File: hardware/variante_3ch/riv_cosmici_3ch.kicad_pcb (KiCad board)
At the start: 2 copper layers, 103 x 223.9 mm, 214 parts, among them J101 SiPM_CH1, J104 LEMO_CH1, J201 SiPM_CH2, J204 LEMO_CH2, J3 PWR_5V, J301 SiPM_CH3, J304 LEMO_CH3, J5 LEMO_AND, J6 I2C_RPI, Q101 BFR93A, Q102 MMBTH81, Q201 BFR93A, Q202 MMBTH81, Q301 BFR93A, Q302 MMBTH81, U1 LT3461, U10 74LVC1G11, U102 TLC555/LMC555, U103 MAX961, U108 LT1636, U109 74LVC1G17, U11 MCP3424, U12 MCP3424, U202 TLC555/LMC555, U203 MAX961, U208 LT1636, U209 74LVC1G17, U302 TLC555/LMC555, U303 MAX961, U308 LT1636, U309 74LVC1G17, U5 LP2985AIM5-3.6, U6 MCP1825S-3302, U7 LP2985AIM5-3.6

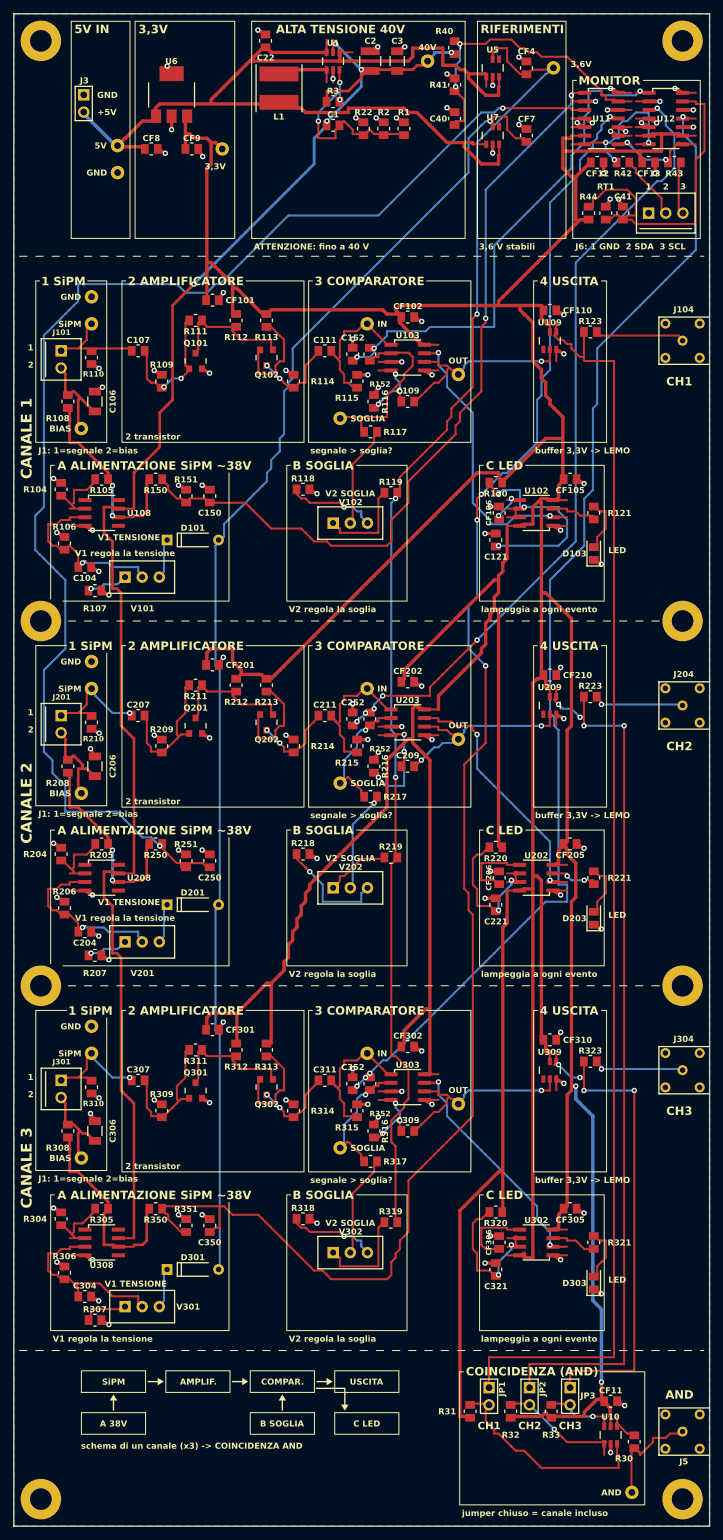
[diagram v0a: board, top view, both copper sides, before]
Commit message: Scheda a 3 canali: protezione dell'alimentazione (USB-C, fusibile, TVS, MOSFET P, LED)
USB-C solo alimentazione J7 (GCT USB4125-GF-A, 5,1k su CC) o J3 da banco ->
fusibile ripristinabile F1 (MF-MSMF050-2) -> TVS D5 (SMAJ5.0A) -> MOSFET P Q4
(AO3401A, inversione di polarita') -> +5V; C60 10 uF e LED di accensione D6.
Generatore: piazzole con asola (guscio USB-C) in PCB KiCad, Gerber e foratura (G85);
nuovi simboli e impronte (dalla libreria KiCad 7.0.11); routing aggiunto senza toccare
le altre reti. Verifica KiCad: schema = PCB, DRC senza errori, 0 reti spezzate.
Simulazione ngspice della scheda intera: +5V 4,977 V, il resto invariato.
Schema A4: nuovo foglio 2 (ingresso e protezione); nota per il tecnico INFN aggiornata.

Co-Authored-By: Claude Opus 5.5 <noreply@anthropic.com>
Claude-Session: https://claude.ai/code/session_017fc9yPsNewCQrMK8R1c8Ls
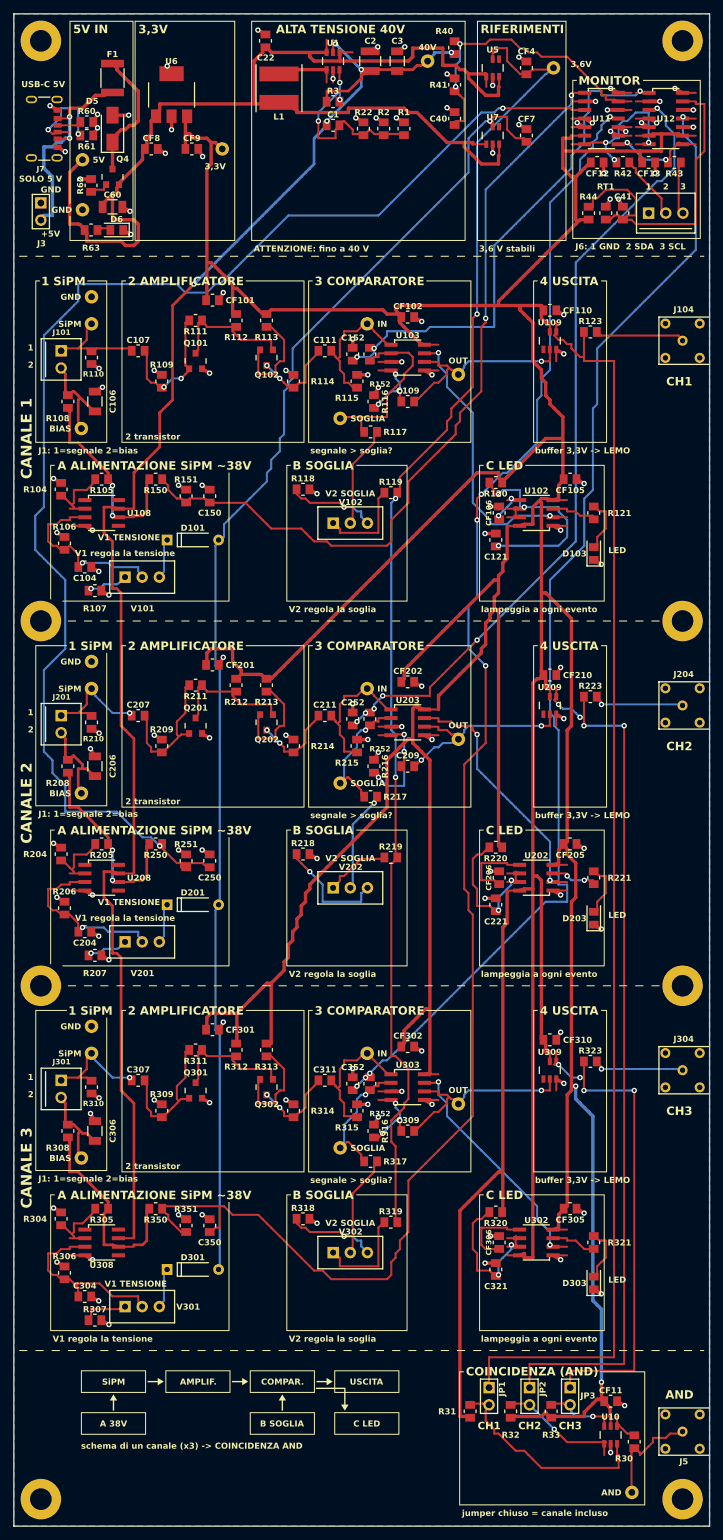
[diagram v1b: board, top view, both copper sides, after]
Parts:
- added C60: 10u, rivlib:C_1206, F.Cu at (34.6, 48.6)
- added D5: SMAJ5.0A, rivlib:D_SMA, F.Cu at (34.6, 37.0)
- added D6: LED verde, rivlib:LED_0805, F.Cu at (35.2, 52.0)
- added F1: MF-MSMF050-2, rivlib:F_1812, F.Cu at (34.6, 29.5)
- added J7: USB_C_PWR, rivlib:USBC_GCT_USB4125, F.Cu at (23.4, 37.0)
- added Q4: AO3401A, rivlib:SOT23, F.Cu at (34.6, 44.1)
- added R60: 5k1, rivlib:R_0805, F.Cu at (30.8, 36.0)
- added R61: 5k1, rivlib:R_0805, F.Cu at (30.8, 38.0)
- added R62: 10k, rivlib:R_0805, F.Cu at (31.4, 45.4)
- added R63: 1k5, rivlib:R_0805, F.Cu at (31.4, 52.0)
- moved J3 17.2 mm to (24.0, 48.0)
- moved TP6 7.56 mm to (30.2, 49.0)
- moved TP2 5.60 mm to (30.2, 41.6)
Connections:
- J3 pad 2: +5V -> /VIN_RAW
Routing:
- net /VIN_RAW: track 0.00 -> 31.8 mm, vias 0 -> 2
- net +5V: track 157.8 -> 178.4 mm
- net /VIN_F: track 0.00 -> 19.4 mm
- net /CC2: track 0.00 -> 14.6 mm, vias 0 -> 2
- net GND: track 225.2 -> 238.1 mm, vias 117 -> 125
- net /CC1: track 0.00 -> 3.65 mm
- net /Q4_G: track 0.00 -> 2.82 mm
- net /LED_PWR: track 0.00 -> 2.04 mm
